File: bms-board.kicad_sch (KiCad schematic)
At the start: 1 part, among them U1 LTC6804-2

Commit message: Merging new develop into new feature (#6)
* feat: add 6804-2 kicad symbol

* TEMPLATE: add pull request description template

* feat: add automated git flow setup script

* update feature/our-symbol-library branch to latest develop edition (#5)

* TEMPLATE: add pull request description template

* feat: add automated git flow setup script

* feat: a maybe working fixed wing schematic symbol library

* feat: add line to checkout dev branch when running setup script

* feat: fix FixedWing symbol library to include LTC6804-2

* refactor: verifying symbol library works, remove individual ltc6804-2 symbol

* feat: adding needed files

* feat: edit conflict in setup script

---------

Co-authored-by: Ephram Cola Jacquin <89238547+ephram2004@users.noreply.github.com>
Co-authored-by: Ephram Cola Jacquin <ecolajacquin@gmail.com>
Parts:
- added U2: LTC6804-2, Package_SO:SSOP-48_5.3x12.8mm_P0.5mm, symbol FixedWing:LTC6804-2
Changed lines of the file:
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@@
 (kicad_sch (version 20230121) (generator eeschema)
   (paper "A4")
+  (symbol (lib_id "FixedWing:LTC6804-2") (at 111.76 93.98 0) (unit 1)
+    (in_bom yes) (on_board yes) (dnp no) (fields_autoplaced)
+    (property "Reference" "U2" (at 111.76 55.88 0)
+      (effects (font (size 1.27 1.27)))
+    )
+    (property "Value" "LTC6804-2" (at 111.76 58.42 0)
+      (effects (font (size 1.27 1.27)))
+    )
+    (property "Footprint" "Package_SO:SSOP-48_5.3x12.8mm_P0.5mm" (at 111.76 132.08 0)
+      (effects (font (size 1.27 1.27)) hide)
+    )
+    (property "Datasheet" "https://www.analog.com/media/en/technical-documentation/data-sheets/680412fc.pdf" (at 114.3 57.15 0)
+      (effects (font (size 1.27 1.27)) hide)
+    )
+    (pin "44")
+    (pin "11")
+    (pin "12")
+    (pin "36")
+    (pin "37")
+    (pin "4")
+    (pin "14")
+    (pin "41")
+    (pin "10")
+    (pin "2")
+    (pin "22")
+    (pin "40")
+    (pin "46")
+    (pin "5")
+    (pin "29")
+    (pin "9")
+    (pin "24")
+    (pin "21")
+    (pin "31")
+    (pin "42")
+    (pin "47")
+    (pin "13")
+    (pin "3")
+    (pin "48")
+    (pin "6")
+    (pin "32")
+    (pin "34")
+    (pin "20")
+    (pin "8")
+    (pin "1")
+    (pin "28")
+    (pin "19")
+    (pin "26")
+    (pin "15")
+    (pin "38")
+    (pin "16")
+    (pin "35")
+    (pin "43")
+    (pin "33")
+    (pin "17")
+    (pin "18")
+    (pin "25")
+    (pin "45")
+    (pin "7")
+    (pin "23")
+    (pin "30")
+    (pin "27")
+    (pin "39")
+    (instances
+      (project "bms-board"
+        (path "/8a7831d1-a913-4f04-8780-225d2234b41d"
+          (reference "U2") (unit 1)
+        )
+      )
+    )
+  )
   (symbol (lib_id "Battery_Management:LTC6804-2") (at 148.59 92.71 0) (unit 1)
     (in_bom yes) (on_board yes) (dnp no) (fields_autoplaced)

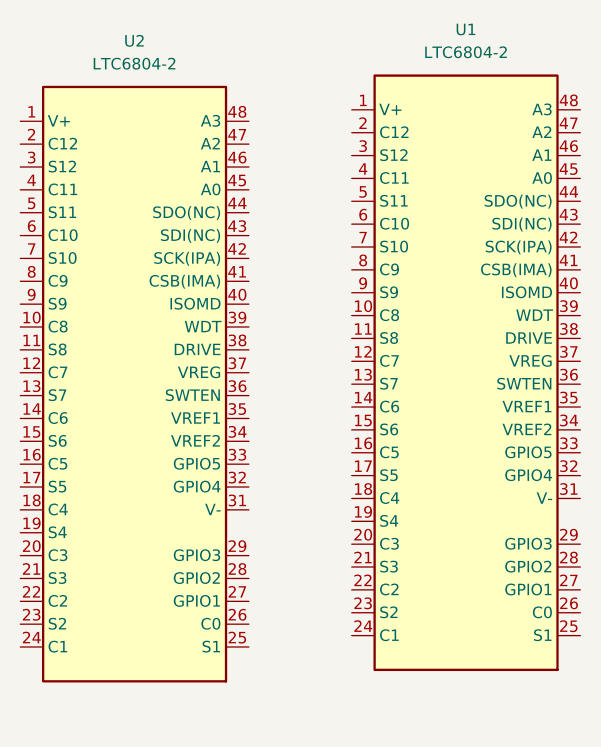
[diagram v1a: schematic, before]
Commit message: fix: changed symbol for easier schematic design and orginization by pin logic
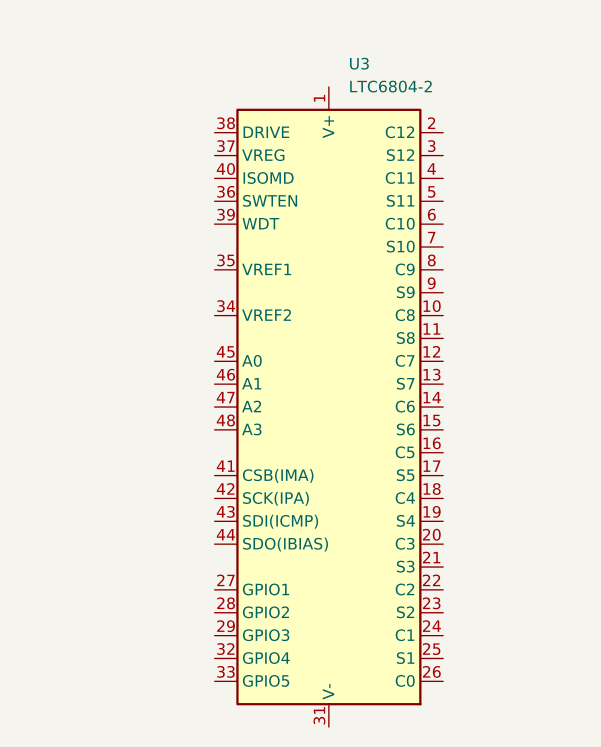
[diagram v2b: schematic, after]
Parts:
- removed U1: LTC6804-2, Package_SO:SSOP-48_5.3x12.8mm_P0.5mm, symbol Battery_Management:LTC6804-2
- removed U2: LTC6804-2, Package_SO:SSOP-48_5.3x12.8mm_P0.5mm, symbol FixedWing:LTC6804-2
- added U3: LTC6804-2, Package_SO:SSOP-48_5.3x12.8mm_P0.5mm, symbol FixedWing:LTC6804-2
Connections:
- new net: U3.30 (V-), U3.31 (V-)
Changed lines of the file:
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@@
 (kicad_sch (version 20230121) (generator eeschema)
   (paper "A4")
-  (symbol (lib_id "FixedWing:LTC6804-2") (at 111.76 93.98 0) (unit 1)
+  (symbol (lib_name "LTC6804-2_1") (lib_id "FixedWing:LTC6804-2") (at 133.35 96.52 0) (unit 1)
     (in_bom yes) (on_board yes) (dnp no) (fields_autoplaced)
-    (property "Reference" "U2" (at 111.76 55.88 0)
-      (effects (font (size 1.27 1.27)))
+    (property "Reference" "U3" (at 135.5441 58.42 0)
+      (effects (font (size 1.27 1.27)) (justify left))
     )
-    (property "Value" "LTC6804-2" (at 111.76 58.42 0)
-      (effects (font (size 1.27 1.27)))
+    (property "Value" "LTC6804-2" (at 135.5441 60.96 0)
+      (effects (font (size 1.27 1.27)) (justify left))
     )
-    (property "Footprint" "Package_SO:SSOP-48_5.3x12.8mm_P0.5mm" (at 111.76 132.08 0)
+    (property "Footprint" "Package_SO:SSOP-48_5.3x12.8mm_P0.5mm" (at 133.35 133.35 0)
       (effects (font (size 1.27 1.27)) hide)
     )
-    (property "Datasheet" "https://www.analog.com/media/en/technical-documentation/data-sheets/680412fc.pdf" (at 114.3 57.15 0)
+    (property "Datasheet" "https://www.analog.com/media/en/technical-documentation/data-sheets/680412fc.pdf" (at 147.32 62.23 0)
       (effects (font (size 1.27 1.27)) hide)
     )
-    (pin "44")
+    (pin "37")
+    (pin "2")
+    (pin "39")
+    (pin "32")
+    (pin "36")
+    (pin "4")
+    (pin "41")
     (pin "11")
+    (pin "20")
     (pin "12")
-    (pin "36")
-    (pin "37")
-    (pin "4")
+    (pin "21")
+    (pin "30")
+    (pin "33")
+    (pin "16")
+    (pin "19")
+    (pin "34")
+    (pin "40")
+    (pin "1")
+    (pin "13")
+    (pin "17")
+    (pin "10")
+    (pin "18")
+    (pin "22")
+    (pin "26")
+    (pin "23")
+    (pin "24")
+    (pin "28")
+    (pin "15")
     (pin "14")
-    (pin "41")
-    (pin "10")
-    (pin "2")
-    (pin "22")
-    (pin "40")
-    (pin "46")
+    (pin "27")
+    (pin "25")
+    (pin "29")
+    (pin "3")
+    (pin "35")
+    (pin "31")
+    (pin "38")
     (pin "5")
-    (pin "29")
-    (pin "9")
-    (pin "24")
-    (pin "21")
-    (pin "31")
     (pin "42")
-    (pin "47")
-    (pin "13")
-    (pin "3")
+    (pin "43")
     (pin "48")
     (pin "6")
-    (pin "32")
-    (pin "34")
-    (pin "20")
+    (pin "7")
+    (pin "45")
     (pin "8")
-    (pin "1")
-    (pin "28")
-    (pin "19")
-    (pin "26")
-    (pin "15")
-    (pin "38")
-    (pin "16")
-    (pin "35")
-    (pin "43")
-    (pin "33")
-    (pin "17")
-    (pin "18")
-    (pin "25")
-    (pin "45")
-    (pin "7")
-    (pin "23")
-    (pin "30")
-    (pin "27")
-    (pin "39")
+    (pin "9")
+    (pin "46")
+    (pin "47")
+    (pin "44")
     (instances
       (project "bms-board"
         (path "/8a7831d1-a913-4f04-8780-225d2234b41d"
-          (reference "U2") (unit 1)
+          (reference "U3") (unit 1)
         )
       )
-    )
-  )
-  (symbol (lib_id "Battery_Management:LTC6804-2") (at 148.59 92.71 0) (unit 1)
-    (in_bom yes) (on_board yes) (dnp no) (fields_autoplaced)
-    (property "Reference" "U1" (at 148.59 54.61 0)
-      (effects (font (size 1.27 1.27)))
-    )
-    (property "Value" "LTC6804-2" (at 148.59 57.15 0)
-      (effects (font (size 1.27 1.27)))
-    )
-    (property "Footprint" "Package_SO:SSOP-48_5.3x12.8mm_P0.5mm" (at 148.59 130.81 0)
-      (effects (font (size 1.27 1.27)) hide)
-    )
-    (property "Datasheet" "https://www.analog.com/media/en/technical-documentation/data-sheets/680412fc.pdf" (at 151.13 55.88 0)
-      (effects (font (size 1.27 1.27)) hide)
-    )
-    (pin "19")
-    (pin "20")
-    (pin "17")
-    (pin "21")
-    (pin "39")
-    (pin "40")
-    (pin "16")
-    (pin "15")
-    (pin "22")
-    (pin "12")
-    (pin "44")
-    (pin "45")
-    (pin "46")
-    (pin "47")
-    (pin "48")
-    (pin "23")
-    (pin "4")
-    (pin "11")
-    (pin "10")
-    (pin "5")
-    (pin "6")
-    (pin "7")
-    (pin "8")
-    (pin "9")
-    (pin "1")
-    (pin "24")
-    (pin "25")
-    (pin "26")
-    (pin "27")
-    (pin "28")
-    (pin "29")
-    (pin "3")
-    (pin "30")
-    (pin "31")
-    (pin "32")
-    (pin "33")
-    (pin "34")
-    (pin "35")
-    (pin "36")
-    (pin "37")
-    (pin "38")
-    (pin "13")
-    (pin "18")
-    (pin "2")
-    (pin "14")
-    (pin "41")
-    (pin "42")
-    (pin "43")
-    (instances
-      (project "bms-board"
-        (path "/8a7831d1-a913-4f04-8780-225d2234b41d"
-          (reference "U1") (unit 1)
-        )
-      )
